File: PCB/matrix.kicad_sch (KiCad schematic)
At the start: 99 parts, among them SW10 EC_SW, SW100 EC_SW, SW11 EC_SW, SW12 EC_SW, SW13 EC_SW, SW14 EC_SW, SW15 EC_SW, SW16 EC_SW, SW17 EC_SW, SW18 EC_SW, SW19 EC_SW, SW2 EC_SW, SW20 EC_SW, SW21 EC_SW, SW22 EC_SW, SW23 EC_SW, SW24 EC_SW, SW25 EC_SW, SW26 EC_SW, SW27 EC_SW, SW28 EC_SW, SW29 EC_SW, SW3 EC_SW, SW30 EC_SW, SW31 1U, SW32 2U, SW33 1U, SW34 EC_SW, SW35 EC_SW, SW36 EC_SW, SW37 EC_SW, SW38 EC_SW, SW39 EC_SW, SW4 EC_SW, SW40 EC_SW, SW41 EC_SW, SW42 EC_SW, SW43 EC_SW, SW44 EC_SW, SW45 EC_SW, SW46 EC_SW, SW47 EC_SW, SW48 EC_SW, SW49 EC_SW, SW5 EC_SW, SW50 ANSI_\, SW51 ANSI_Enter, SW52 EC_SW, SW53 EC_SW, SW54 EC_SW, SW55 EC_SW, SW56 EC_SW, SW57 EC_SW, SW58 EC_SW, SW59 EC_SW, SW6 EC_SW, SW60 EC_SW, SW61 EC_SW, SW62 EC_SW, SW63 EC_SW, SW64 EC_SW, SW65 EC_SW, SW66 EC_SW, SW67 ISO_|, SW68 ANSI_Enter, SW69 1.25U, SW7 EC_SW, SW70 2.25U, SW71 1U, SW72 EC_SW, SW73 EC_SW, SW74 EC_SW, SW75 EC_SW, SW76 EC_SW, SW77 EC_SW, SW78 EC_SW, SW79 EC_SW, SW8 EC_SW, SW80 EC_SW, SW81 EC_SW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

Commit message: Update
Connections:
- net COL0: now also SW55.1, SW70.1; no longer SW55.2, SW70.2
- net ROW3: now also SW55.2; no longer SW55.1
- net ROW4: now also SW70.2; no longer SW70.1
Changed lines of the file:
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@@
     (pin "3")
   )
-  (symbol (lib_id "cipulot_parts:EC_SW") (at 46.355 165.1 0) (unit 1)
+  (symbol (lib_id "cipulot_parts:EC_SW") (at 46.355 165.1 0) (mirror y) (unit 1)
     (in_bom yes) (on_board yes) (fields_autoplaced)
     (property "Reference" "SW70" (id 0) (at 46.355 159.2412 0))
@@
     (pin "1")
   )
-  (symbol (lib_id "cipulot_parts:EC_SW") (at 46.355 149.225 0) (unit 1)
+  (symbol (lib_id "cipulot_parts:EC_SW") (at 46.355 149.225 0) (mirror y) (unit 1)
     (in_bom yes) (on_board yes) (fields_autoplaced)
     (property "Reference" "SW55" (id 0) (at 46.355 143.3662 0))

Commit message: Update and pre-production output
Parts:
- SW70, SW71: footprint cipulot_parts:ecs_pad_no_ring_1u_edge_cut -> cipulot_parts:ecs_pad_no_ring
- SW90, SW93: footprint cipulot_parts:ecs_pad_no_ring_stepped&normal -> cipulot_parts:ecs_pad_no_ring_stepped&normal_cut
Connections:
- net COL6: now also SW90.1; no longer SW90.2
- net ROW1: now also SW36.1; no longer SW35.1
- net ROW2: now also SW35.1; no longer SW36.1
- net ROW3: now also SW54.1; no longer SW53.1
- net ROW4: now also SW53.1; no longer SW54.1
- net ROW5: now also SW90.2, SW95.1; no longer SW90.1
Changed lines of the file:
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@@
   (title_block
     (title "RF_R1_8-9Xu PCB - Matrix")
-    (date "2022-08-01")
+    (date "2022-08-09")
     (rev "1")
     (company "Cipulot PCB Design ")
@@
   (junction (at 236.855 137.795) (diameter 0) (color 0 0 0 0)
   )
+  (junction (at 340.36 146.685) (diameter 0) (color 0 0 0 0)
+  )
   (junction (at 65.405 106.68) (diameter 0) (color 0 0 0 0)
   )
@@
   (junction (at 76.835 123.825) (diameter 0) (color 0 0 0 0)
   )
-  (junction (at 340.36 143.51) (diameter 0) (color 0 0 0 0)
-  )
   (junction (at 149.225 132.715) (diameter 0) (color 0 0 0 0)
   )
@@
   (junction (at 141.605 122.555) (diameter 0) (color 0 0 0 0)
   )
-  (junction (at 342.265 146.685) (diameter 0) (color 0 0 0 0)
-  )
   (junction (at 320.675 132.715) (diameter 0) (color 0 0 0 0)
   )
@@
   (junction (at 263.525 165.1) (diameter 0) (color 0 0 0 0)
   )
+  (junction (at 248.285 187.325) (diameter 0) (color 0 0 0 0)
+  )
   (junction (at 114.935 123.825) (diameter 0) (color 0 0 0 0)
   )
@@
   (junction (at 217.805 154.305) (diameter 0) (color 0 0 0 0)
   )
+  (junction (at 342.265 143.51) (diameter 0) (color 0 0 0 0)
+  )
   (junction (at 122.555 154.305) (diameter 0) (color 0 0 0 0)
   )
@@
     (stroke (width 0) (type default) (color 0 0 0 0))
   )
-  (wire (pts (xy 340.36 143.51) (xy 365.76 143.51))
-    (stroke (width 0) (type default) (color 0 0 0 0))
-  )
   (wire (pts (xy 172.085 172.085) (xy 191.135 172.085))
     (stroke (width 0) (type default) (color 0 0 0 0))
@@
     (stroke (width 0) (type default) (color 0 0 0 0))
   )
+  (wire (pts (xy 340.36 146.685) (xy 340.36 156.21))
+    (stroke (width 0) (type default) (color 0 0 0 0))
+  )
   (wire (pts (xy 316.865 172.085) (xy 286.385 172.085))
     (stroke (width 0) (type default) (color 0 0 0 0))
@@
     (stroke (width 0) (type default) (color 0 0 0 0))
   )
+  (wire (pts (xy 342.265 143.51) (xy 342.265 172.085))
+    (stroke (width 0) (type default) (color 0 0 0 0))
+  )
   (wire (pts (xy 217.805 170.18) (xy 236.855 170.18))
     (stroke (width 0) (type default) (color 0 0 0 0))
@@
     (stroke (width 0) (type default) (color 0 0 0 0))
   )
-  (wire (pts (xy 340.36 143.51) (xy 340.36 156.21))
+  (wire (pts (xy 340.36 117.475) (xy 340.36 146.685))
     (stroke (width 0) (type default) (color 0 0 0 0))
   )
@@
     (stroke (width 0) (type default) (color 0 0 0 0))
   )
+  (wire (pts (xy 383.54 123.825) (xy 383.54 117.475))
+    (stroke (width 0) (type default) (color 0 0 0 0))
+  )
   (wire (pts (xy 381 88.9) (xy 381 101.6))
     (stroke (width 0) (type default) (color 0 0 0 0))
@@
     (stroke (width 0) (type default) (color 0 0 0 0))
   )
-  (wire (pts (xy 365.76 123.825) (xy 337.82 123.825))
-    (stroke (width 0) (type default) (color 0 0 0 0))
-  )
   (wire (pts (xy 286.385 123.825) (xy 305.435 123.825))
     (stroke (width 0) (type default) (color 0 0 0 0))
@@
     (stroke (width 0) (type default) (color 0 0 0 0))
   )
+  (wire (pts (xy 365.76 125.095) (xy 323.215 125.095))
+    (stroke (width 0) (type default) (color 0 0 0 0))
+  )
   (wire (pts (xy 133.985 140.335) (xy 153.035 140.335))
     (stroke (width 0) (type default) (color 0 0 0 0))
@@
     (stroke (width 0) (type default) (color 0 0 0 0))
   )
+  (wire (pts (xy 340.36 146.685) (xy 384.81 146.685))
+    (stroke (width 0) (type default) (color 0 0 0 0))
+  )
   (wire (pts (xy 76.835 117.475) (xy 76.835 123.825))
     (stroke (width 0) (type default) (color 0 0 0 0))
@@
     (stroke (width 0) (type default) (color 0 0 0 0))
   )
-  (wire (pts (xy 383.54 117.475) (xy 383.54 125.095))
+  (wire (pts (xy 361.95 173.99) (xy 282.575 173.99))
     (stroke (width 0) (type default) (color 0 0 0 0))
   )
-  (wire (pts (xy 361.95 173.99) (xy 282.575 173.99))
+  (wire (pts (xy 365.76 117.475) (xy 365.76 125.095))
     (stroke (width 0) (type default) (color 0 0 0 0))
   )
@@
     (stroke (width 0) (type default) (color 0 0 0 0))
   )
-  (wire (pts (xy 365.76 117.475) (xy 365.76 123.825))
-    (stroke (width 0) (type default) (color 0 0 0 0))
-  )
   (wire (pts (xy 255.905 106.68) (xy 274.955 106.68))
     (stroke (width 0) (type default) (color 0 0 0 0))
@@
     (stroke (width 0) (type default) (color 0 0 0 0))
   )
+  (wire (pts (xy 342.265 143.51) (xy 365.76 143.51))
+    (stroke (width 0) (type default) (color 0 0 0 0))
+  )
   (wire (pts (xy 365.76 187.325) (xy 384.81 187.325))
     (stroke (width 0) (type default) (color 0 0 0 0))
@@
     (stroke (width 0) (type default) (color 0 0 0 0))
   )
-  (wire (pts (xy 229.235 187.325) (xy 344.805 187.325))
+  (wire (pts (xy 248.285 180.975) (xy 248.285 187.325))
+    (stroke (width 0) (type default) (color 0 0 0 0))
+  )
+  (wire (pts (xy 229.235 187.325) (xy 248.285 187.325))
     (stroke (width 0) (type default) (color 0 0 0 0))
   )
@@
     (stroke (width 0) (type default) (color 0 0 0 0))
   )
-  (wire (pts (xy 340.36 117.475) (xy 340.36 143.51))
-    (stroke (width 0) (type default) (color 0 0 0 0))
-  )
   (wire (pts (xy 38.735 156.21) (xy 57.785 156.21))
     (stroke (width 0) (type default) (color 0 0 0 0))
@@
     (stroke (width 0) (type default) (color 0 0 0 0))
   )
-  (wire (pts (xy 342.265 146.685) (xy 342.265 172.085))
+  (wire (pts (xy 342.265 132.715) (xy 342.265 143.51))
     (stroke (width 0) (type default) (color 0 0 0 0))
   )
@@
     (stroke (width 0) (type default) (color 0 0 0 0))
   )
+  (wire (pts (xy 337.82 123.825) (xy 383.54 123.825))
+    (stroke (width 0) (type default) (color 0 0 0 0))
+  )
   (wire (pts (xy 187.325 88.9) (xy 187.325 101.6))
     (stroke (width 0) (type default) (color 0 0 0 0))
@@
     (stroke (width 0) (type default) (color 0 0 0 0))
   )
-  (wire (pts (xy 383.54 125.095) (xy 323.215 125.095))
-    (stroke (width 0) (type default) (color 0 0 0 0))
-  )
   (wire (pts (xy 38.735 123.825) (xy 57.785 123.825))
     (stroke (width 0) (type default) (color 0 0 0 0))
@@
     (stroke (width 0) (type default) (color 0 0 0 0))
   )
+  (wire (pts (xy 248.285 187.325) (xy 344.805 187.325))
+    (stroke (width 0) (type default) (color 0 0 0 0))
+  )
   (wire (pts (xy 65.405 186.055) (xy 84.455 186.055))
     (stroke (width 0) (type default) (color 0 0 0 0))
@@
     (stroke (width 0) (type default) (color 0 0 0 0))
   )
-  (wire (pts (xy 342.265 132.715) (xy 342.265 146.685))
-    (stroke (width 0) (type default) (color 0 0 0 0))
-  )
   (wire (pts (xy 191.135 156.21) (xy 210.185 156.21))
     (stroke (width 0) (type default) (color 0 0 0 0))
@@
     (stroke (width 0) (type default) (color 0 0 0 0))
   )
-  (wire (pts (xy 384.81 146.685) (xy 342.265 146.685))
-    (stroke (width 0) (type default) (color 0 0 0 0))
-  )
   (wire (pts (xy 191.135 140.335) (xy 210.185 140.335))
     (stroke (width 0) (type default) (color 0 0 0 0))
@@
     (property "Reference" "SW93" (id 0) (at 217.805 175.1162 0))
     (property "Value" "EC_SW" (id 1) (at 217.805 177.6531 0))
-    (property "Footprint" "cipulot_parts:ecs_pad_no_ring_stepped&normal" (id 2) (at 217.805 180.975 0)
+    (property "Footprint" "cipulot_parts:ecs_pad_no_ring_stepped&normal_cut" (id 2) (at 217.805 180.975 0)
       (effects (font (size 1.27 1.27)) hide)
     )
@@
     (pin "3")
   )
-  (symbol (lib_id "cipulot_parts:EC_SW") (at 160.655 180.975 0) (unit 1)
+  (symbol (lib_id "cipulot_parts:EC_SW") (at 160.655 180.975 0) (mirror y) (unit 1)
     (in_bom yes) (on_board yes) (fields_autoplaced)
     (property "Reference" "SW90" (id 0) (at 160.655 175.1162 0))
     (property "Value" "EC_SW" (id 1) (at 160.655 177.6531 0))
-    (property "Footprint" "cipulot_parts:ecs_pad_no_ring_stepped&normal" (id 2) (at 160.655 180.975 0)
+    (property "Footprint" "cipulot_parts:ecs_pad_no_ring_stepped&normal_cut" (id 2) (at 160.655 180.975 0)
       (effects (font (size 1.27 1.27)) hide)
     )
@@
     (property "Reference" "SW70" (id 0) (at 46.355 159.2412 0))
     (property "Value" "2.25U" (id 1) (at 46.355 161.7781 0))
-    (property "Footprint" "cipulot_parts:ecs_pad_no_ring_1u_edge_cut" (id 2) (at 46.355 165.1 0)
+    (property "Footprint" "cipulot_parts:ecs_pad_no_ring" (id 2) (at 46.355 165.1 0)
       (effects (font (size 1.27 1.27)) hide)
     )
@@
     (property "Reference" "SW71" (id 0) (at 65.405 159.2412 0))
     (property "Value" "1U" (id 1) (at 65.405 161.7781 0))
-    (property "Footprint" "cipulot_parts:ecs_pad_no_ring_1u_edge_cut" (id 2) (at 65.405 165.1 0)
+    (property "Footprint" "cipulot_parts:ecs_pad_no_ring" (id 2) (at 65.405 165.1 0)
       (effects (font (size 1.27 1.27)) hide)
     )

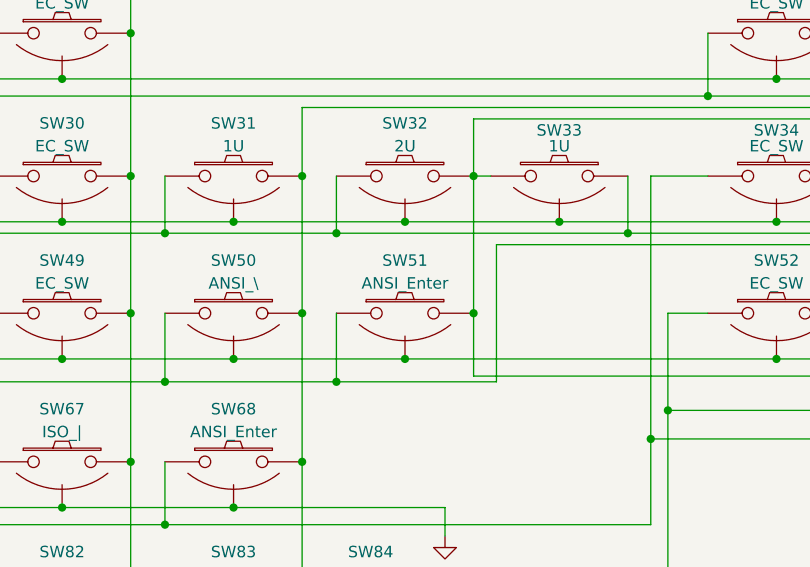
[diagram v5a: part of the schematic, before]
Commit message: Fix in label text
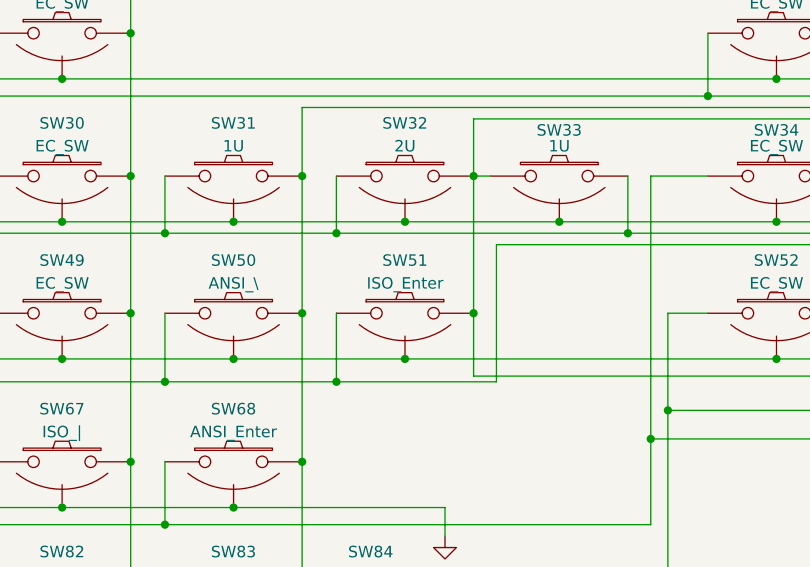
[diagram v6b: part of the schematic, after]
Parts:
- SW51: value ANSI_Enter -> ISO_Enter
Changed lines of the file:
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@@
     (in_bom yes) (on_board yes) (fields_autoplaced)
     (property "Reference" "SW51" (id 0) (at 313.055 126.8562 0))
-    (property "Value" "ANSI_Enter" (id 1) (at 313.055 129.3931 0))
+    (property "Value" "ISO_Enter" (id 1) (at 313.055 129.3931 0))
     (property "Footprint" "cipulot_parts:ecs_pad_no_ring" (id 2) (at 313.055 132.715 0)
       (effects (font (size 1.27 1.27)) hide)

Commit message: Updated footprints and relative models
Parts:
- SW10, SW100, SW11, SW12, SW13, SW14, SW15, SW16, SW17, SW18, SW19, SW2, SW20, SW21, SW22, SW23, SW24, SW25, SW26, SW27, SW28, SW29, SW3, SW30, SW31, SW33, SW34, SW35, SW36, SW37, SW38, SW39, SW4, SW40, SW41, SW42, SW43, SW44, SW45, SW46, SW47, SW48, SW49, SW5, SW50, SW52, SW53, SW54, SW56, SW57, SW58, SW59, SW6, SW60, SW61, SW62, SW63, SW64, SW65, SW66, SW67, SW69, SW7, SW71, SW72, SW73, SW74, SW75, SW76, SW77, SW78, SW79, SW8, SW80, SW81, SW82, SW84, SW85, SW86, SW87, SW88, SW89, SW9, SW91, SW92, SW94, SW95, SW96, SW97, SW98, SW99: footprint cipulot_parts:ecs_pad_no_ring -> cipulot_parts:ecs_pad_1U_no_ring
- SW32, SW51, SW68, SW70, SW83: footprint cipulot_parts:ecs_pad_no_ring -> cipulot_parts:ecs_pad_2U_no_ring
